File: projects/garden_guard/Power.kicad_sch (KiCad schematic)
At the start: 50 parts, among them IC1 ACPL-227-50CE, IC2 INA226AQDGSRQ1, IC3 INA226AQDGSRQ1, J7 USB_C_Receptacle_USB2.0, U10 TPS2121RUXR, U11 MAX20408AFOF, U9 Ag5810

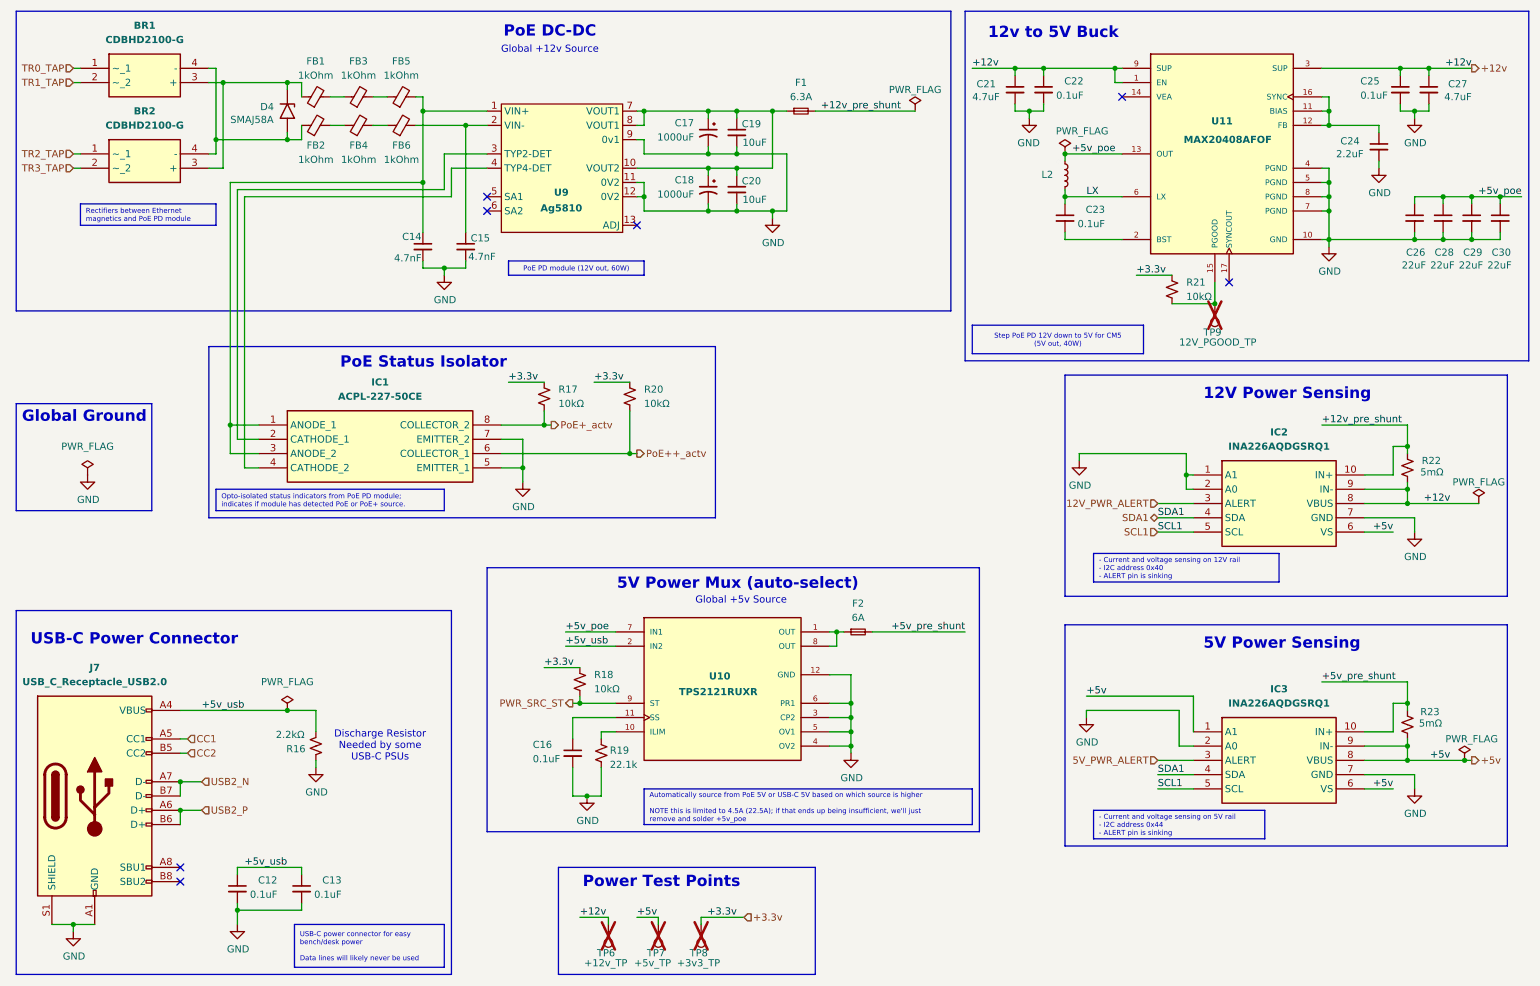
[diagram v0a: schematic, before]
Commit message: JLC part audit - Power - Peripherals - Replace ETQ-P4M2R2KFM with SPM6550T-2R2M-HZ
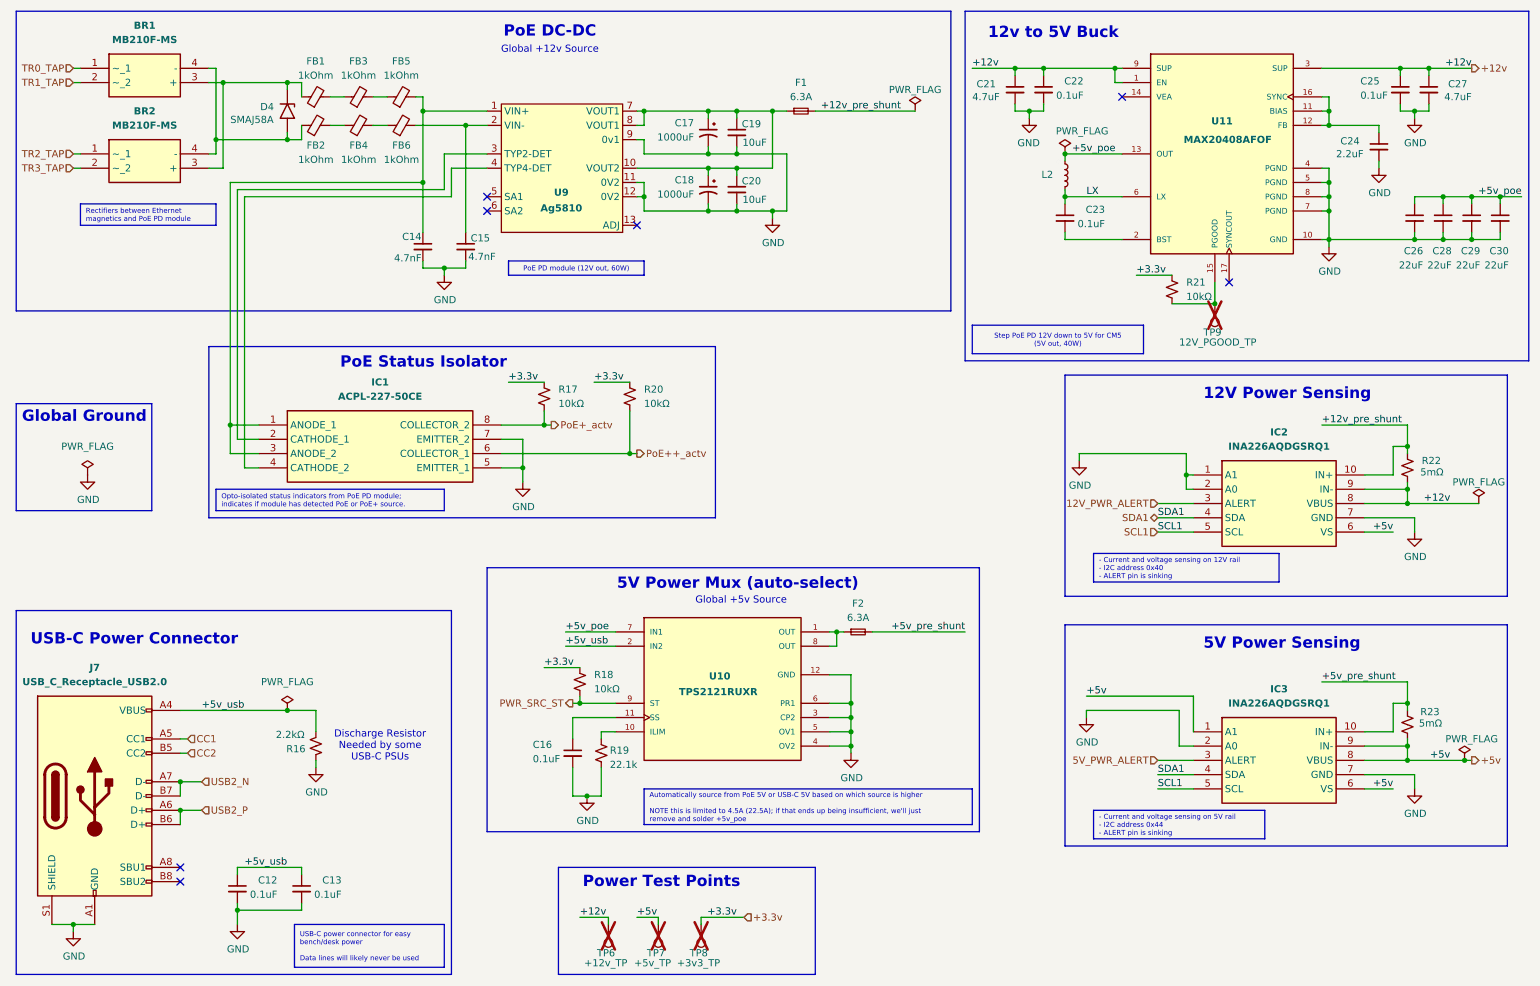
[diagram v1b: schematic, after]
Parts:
- removed BR1, BR2: CDBHD2100-G, Custom_PoE:CDBHD2100-G, symbol Custom_PoE:CDBHD2100-G
- added BR1, BR2: MB210F-MS, Custom_PoE:MB210F-MS, symbol Custom_PoE:MB210F-MS
- C12, C13: footprint Resistor_SMD:R_0603_1608Metric -> Capacitor_SMD:C_0603_1608Metric; Class (none) -> capacitor; Critical (none) -> no; Dielectric_Class (none) -> X7R; JLCPCB_PN (none) -> C2167527; Mfr (none) -> KEMET; Package (none) -> 0603
- C14: Class (none) -> capacitor; Critical (none) -> no; Dielectric_Class (none) -> X7R; JLCPCB_PN (none) -> C2175111; Tolerance (none) -> 10%; Voltage (none) -> 2kV
- C15: Class (none) -> capacitor; Critical (none) -> no; Dielectric_Class (none) -> X7R; JLCPCB_PN (none) -> C2175111; Package (none) -> 1812; Tolerance (none) -> 10%; Voltage (none) -> 2kV
- C16, C23: footprint Resistor_SMD:R_0603_1608Metric -> Capacitor_SMD:C_0603_1608Metric; Class (none) -> capacitor; Critical (none) -> no; Dielectric_Class (none) -> X7R; JLCPCB_PN (none) -> C2167527; Package (none) -> 0603; Tolerance (none) -> 10%; Voltage (none) -> 25V
- C17, C18: Class (none) -> capacitor; Critical (none) -> review; Dielectric_Class (none) -> Electrolytic; JLCPCB_PN (none) -> C401766; Tolerance (none) -> 20%; Voltage (none) -> 25V
- C19, C20: Class (none) -> capacitor; Critical (none) -> no; Dielectric_Class (none) -> X5R; JLCPCB_PN (none) -> C318763; Tolerance (none) -> 20%; Voltage (none) -> 25V
- C21, C27: Class (none) -> capacitor; Critical (none) -> no; Dielectric_Class (none) -> X7R; JLCPCB_PN (none) -> C437556; Package (none) -> 0805
- C22, C25: Class (none) -> capacitor; Critical (none) -> no; Dielectric_Class (none) -> X7R; JLCPCB_PN (none) -> C2167527; Package (none) -> 0603; Tolerance (none) -> 10%; Voltage (none) -> 25V
- C24: Class (none) -> capacitor; Critical (none) -> no; Dielectric_Class (none) -> X5R; JLCPCB_PN (none) -> C77047; Package (none) -> 0603; Tolerance (none) -> 10%; Voltage (none) -> 25V
- C26, C28, C29, C30: Class (none) -> capacitor; Critical (none) -> no; Dielectric_Class (none) -> X5R; JLCPCB_PN (none) -> C45783; MPN GRM219R71E224KA01D -> CL21A226MAQNNNE; Max Temp 125 -> (none); Mfr Murata Electronics -> Samsung; Package (none) -> 0805; Rating None -> (none); Temp Coef X7R -> (none); Tolerance 10% -> 20%
- D4: Class (none) -> tvs; Critical (none) -> review; JLCPCB_PN (none) -> C10762; Mfr Bourns Inc. -> Ruilon
- F1: Class (none) -> fuse; Critical (none) -> review; JLCPCB_PN (none) -> C187567; MPN MFU1206FF06300P500 -> 045806.3DR; Mfr Vishay -> Littelfuse
- F2: value 6A -> 6.3A; footprint Fuse:Fuse_0603_1608Metric -> Fuse:Fuse_1206_3216Metric; Class (none) -> fuse; Critical (none) -> review; JLCPCB_PN (none) -> C187567; MPN JB06F6001R -> 045806.3DR; Mfr YAGEO -> Littelfuse
- FB1, FB2, FB3, FB4, FB5, FB6: Class (none) -> ferrite; Critical (none) -> ferrite; JLCPCB_PN (none) -> C21520; Package (none) -> 1210
- IC1: Class (none) -> opto; Critical (none) -> review; JLCPCB_PN (none) -> zNONE
- IC2: Class (none) -> current_sensor; Critical (none) -> review; JLCPCB_PN (none) -> C2653835
- IC3: Class (none) -> current_sensor; JLCPCB_PN (none) -> C2653835
- J7: Class (none) -> connector; Critical (none) -> yes; Field5 USBF31-0171 -> (none); Field6 USBF31-0171 -> (none); Field7 MTCONN -> (none); JLCPCB_PN (none) -> C45082766; Part Description USBC USB2 data and power connector -> (none)
- L2: value ETQ-P4M2R2KFM -> SPM6550T-2R2M-HZ; footprint Custom_DCDC:ETQ-P4M2R2KFM -> Custom_DCDC:SPM6550T-2R2M-HZ; CREATOR KARTHIK -> (none); Check_prices https://www.snapeda.com/parts/ETQP4M2R2KFM/Panasonic/view-p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 -> (none); Description_1 2.2 µH Shielded Molded Inductor 11.7 A 10.45mOhm Max Nonsta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 -> (none); DigiKey_Part_Number 10-ETQ-P4M2R2KFMCT-ND -> (none); JLCPCB_PN (none) -> C404824; MAXIMUM_PACKAGE_HIEGHT 4.8 mm -> (none); MF Panasonic -> (none); MPN ETQ-P4M2R2KFM -> SPM6550T-2R2M-HZ; Mfr Panasonic -> TDK; PARTREV 19-Dec-25 -> (none); Package NON STANDARD-2 Panasonic -> (none); STANDARD Manufacturer Recommendations -> (none); SnapEDA_Link https://www.snapeda.com/parts/ETQP4M2R2KFM/Panasonic/view-p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 -> (none)
- R16: Class (none) -> resistor; Critical (none) -> no; JLCPCB_PN (none) -> C844925; Mfr Vishay Dale -> Vishay; Package (none) -> 0603; Power 1/8W -> 1/10W; Tolerance (none) -> 1%; Voltage (none) -> 75V
- R17, R18, R20, R21: Class (none) -> resistor; Critical (none) -> no; JLCPCB_PN (none) -> C191124; MPN RC0603FR-0710KL -> ERJ3EKF1002V; Mfr YAGEO -> Panasonic; Package (none) -> 0603; Voltage (none) -> 75V
- R19: Class (none) -> resistor; Critical (none) -> no; JLCPCB_PN (none) -> C25961; MPN RC0603FR-0722K1L -> 0603WAF2212T5E; Mfr YAGEO -> Uniroyal; Package (none) -> 0603; Power (none) -> 1/10W; Voltage (none) -> 75V
- R22, R23: Class (none) -> resistor; Critical (none) -> review; JLCPCB_PN (none) -> C840612; LCSC C840612 -> (none); Package (none) -> 2512; Power (none) -> 3W
- U10: Class (none) -> power_or; Critical (none) -> review; JLCPCB_PN (none) -> C485916; Package VQFN-12 Dialog Semiconductor GmbH -> VQFN-HR-12(2x2.5)
- U11: Class (none) -> buck; Critical (none) -> review; JLCPCB_PN (none) -> zNONE
- U9: Class (none) -> poe; Critical (none) -> yes
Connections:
- net TR0_TAP: now also BR1.1 (~_1)
- net TR1_TAP: now also BR1.2 (~_2)
- net TR2_TAP: now also BR2.1 (~_1)
- net TR3_TAP: now also BR2.2 (~_2)
- net at D4.1 (A1), FB1.1: now also BR1.3 (+), BR2.3 (+)
- net at D4.2 (A2), FB2.1: now also BR1.4 (-), BR2.4 (-)

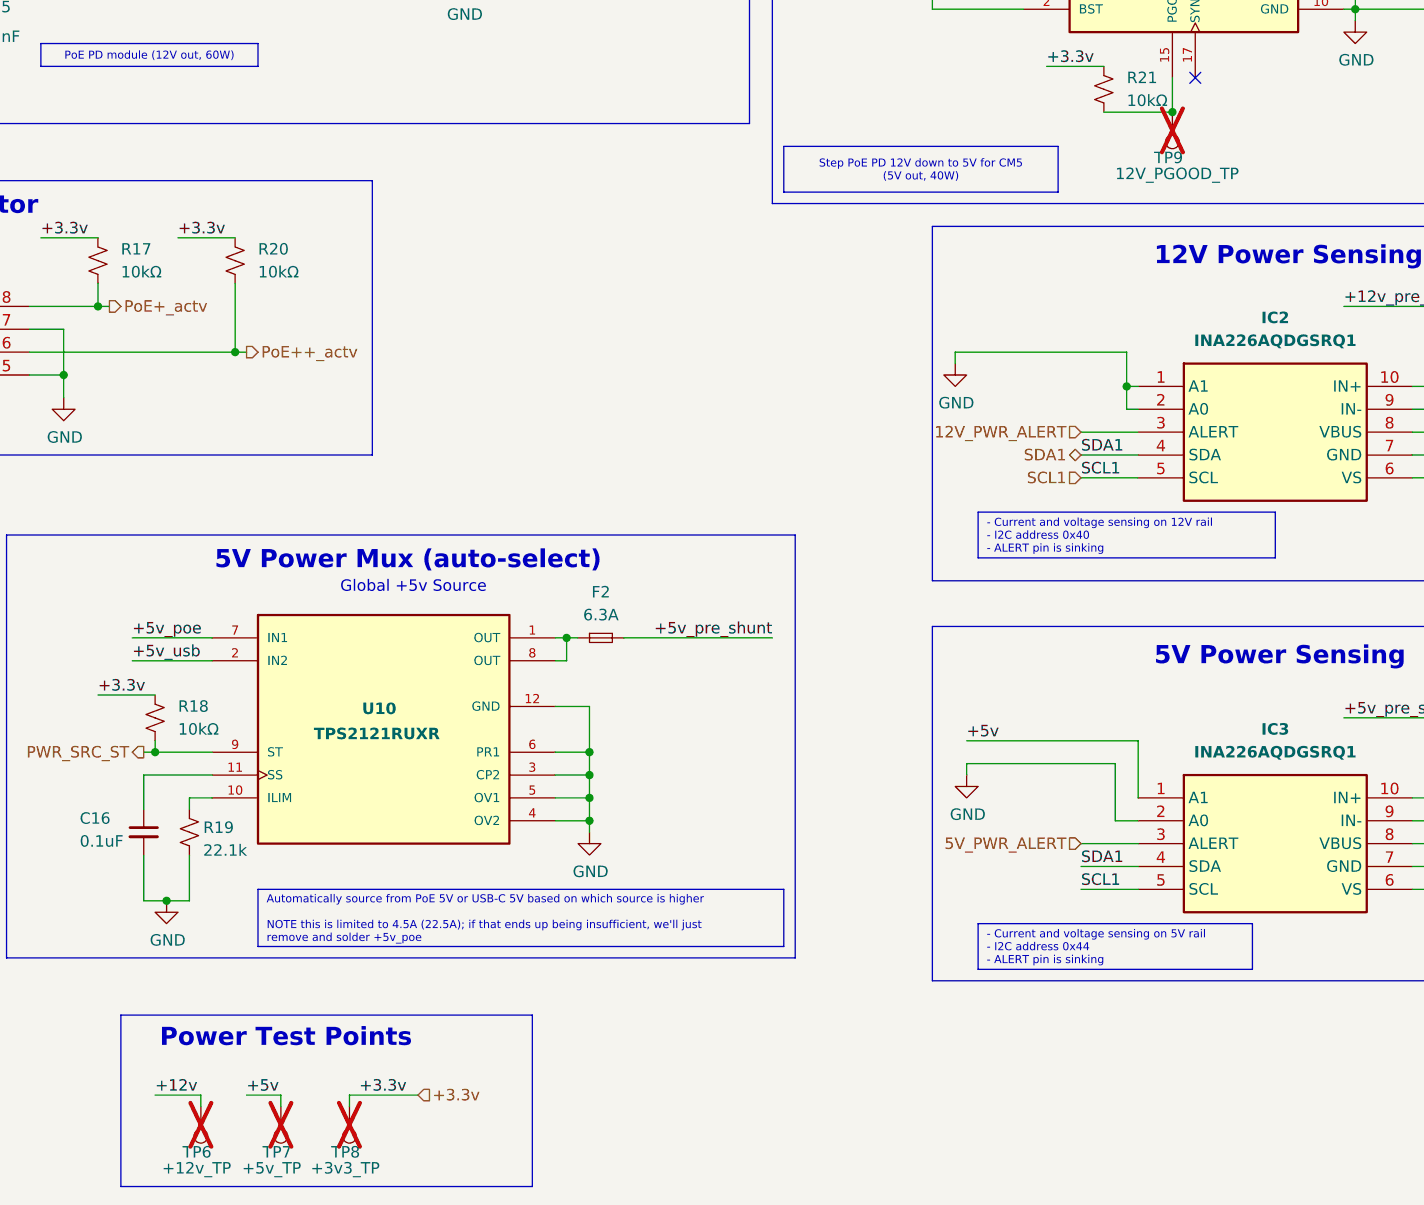
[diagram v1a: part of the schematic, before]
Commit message: - All footprints laid out; DRC NOT run yet, likely has many violations - Thin out peripheral headers, move remaining to dispersed test pads - Update kicad-libraries
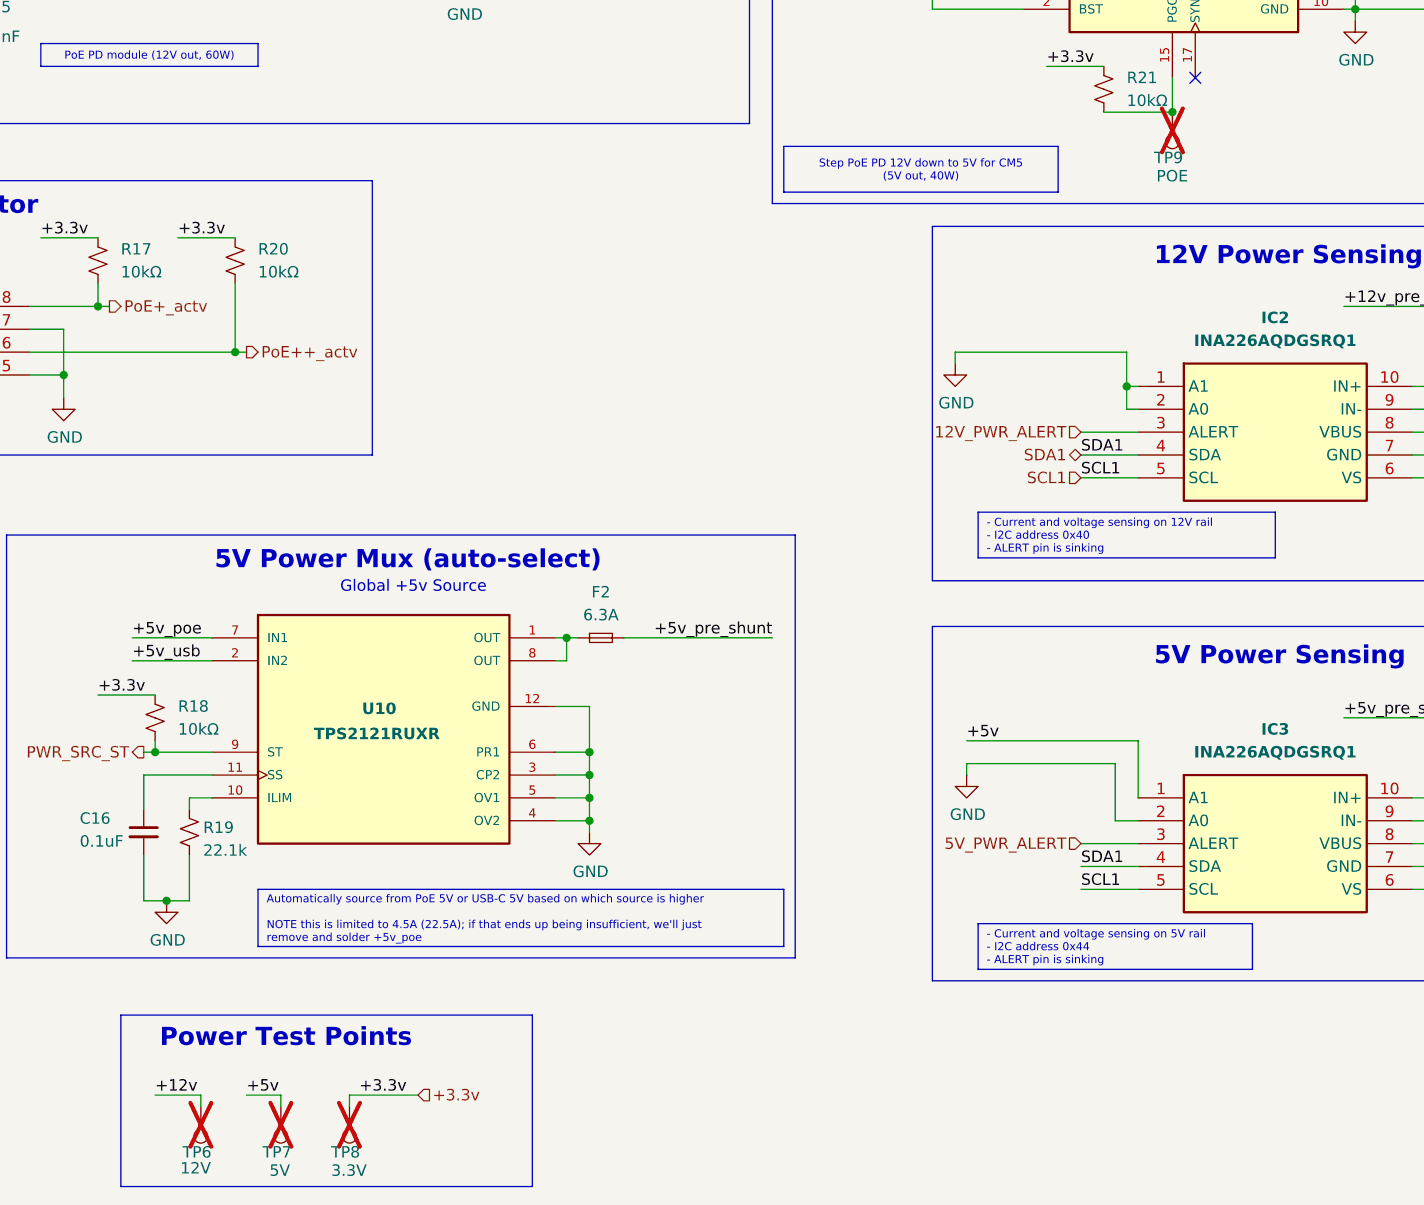
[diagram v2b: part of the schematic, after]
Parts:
- TP6: value +12v_TP -> 12V; footprint TestPoint:TestPoint_Pad_2.0x2.0mm -> TestPoint:TestPoint_Pad_D1.0mm
- TP7: value +5v_TP -> 5V; footprint TestPoint:TestPoint_Pad_2.0x2.0mm -> TestPoint:TestPoint_Pad_D1.0mm
- TP8: value +3v3_TP -> 3.3V; footprint TestPoint:TestPoint_Pad_2.0x2.0mm -> TestPoint:TestPoint_Pad_D1.0mm
- TP9: value 12V_PGOOD_TP -> POE; footprint TestPoint:TestPoint_Pad_2.0x2.0mm -> TestPoint:TestPoint_Pad_D1.0mm
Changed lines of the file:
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@@
 			)
 		)
-		(property "Value" "+5v_TP"
-			(at 123.952 183.388 0)
+		(property "Value" "5V"
+			(at 127 183.642 0)
 			(effects
 				(font
@@
 			)
 		)
-		(property "Footprint" "TestPoint:TestPoint_Pad_2.0x2.0mm"
+		(property "Footprint" "TestPoint:TestPoint_Pad_D1.0mm"
 			(at 123.19 176.53 0)
 			(effects
@@
 			)
 		)
-		(property "Value" "12V_PGOOD_TP"
-			(at 220.98 72.898 0)
+		(property "Value" "POE"
+			(at 225.552 73.152 0)
 			(effects
 				(font
@@
 			)
 		)
-		(property "Footprint" "TestPoint:TestPoint_Pad_2.0x2.0mm"
+		(property "Footprint" "TestPoint:TestPoint_Pad_D1.0mm"
 			(at 222.25 66.04 0)
 			(effects
@@
 			)
 		)
-		(property "Value" "+3v3_TP"
-			(at 131.572 183.388 0)
+		(property "Value" "3.3V"
+			(at 133.858 183.642 0)
 			(effects
 				(font
@@
 			)
 		)
-		(property "Footprint" "TestPoint:TestPoint_Pad_2.0x2.0mm"
+		(property "Footprint" "TestPoint:TestPoint_Pad_D1.0mm"
 			(at 130.81 176.53 0)
 			(effects
@@
 			)
 		)
-		(property "Value" "+12v_TP"
-			(at 115.062 183.388 0)
+		(property "Value" "12V"
+			(at 117.094 183.388 0)
 			(effects
 				(font
@@
 			)
 		)
-		(property "Footprint" "TestPoint:TestPoint_Pad_2.0x2.0mm"
+		(property "Footprint" "TestPoint:TestPoint_Pad_D1.0mm"
 			(at 114.3 176.53 0)
 			(effects
